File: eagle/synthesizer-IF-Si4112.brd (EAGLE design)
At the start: 34 x 31 mm, 39 parts, among them J1 142-0701-851, J3 142-0701-851, Q1 PMOS, U1 SI4112, X1 ECS-TXO-3225

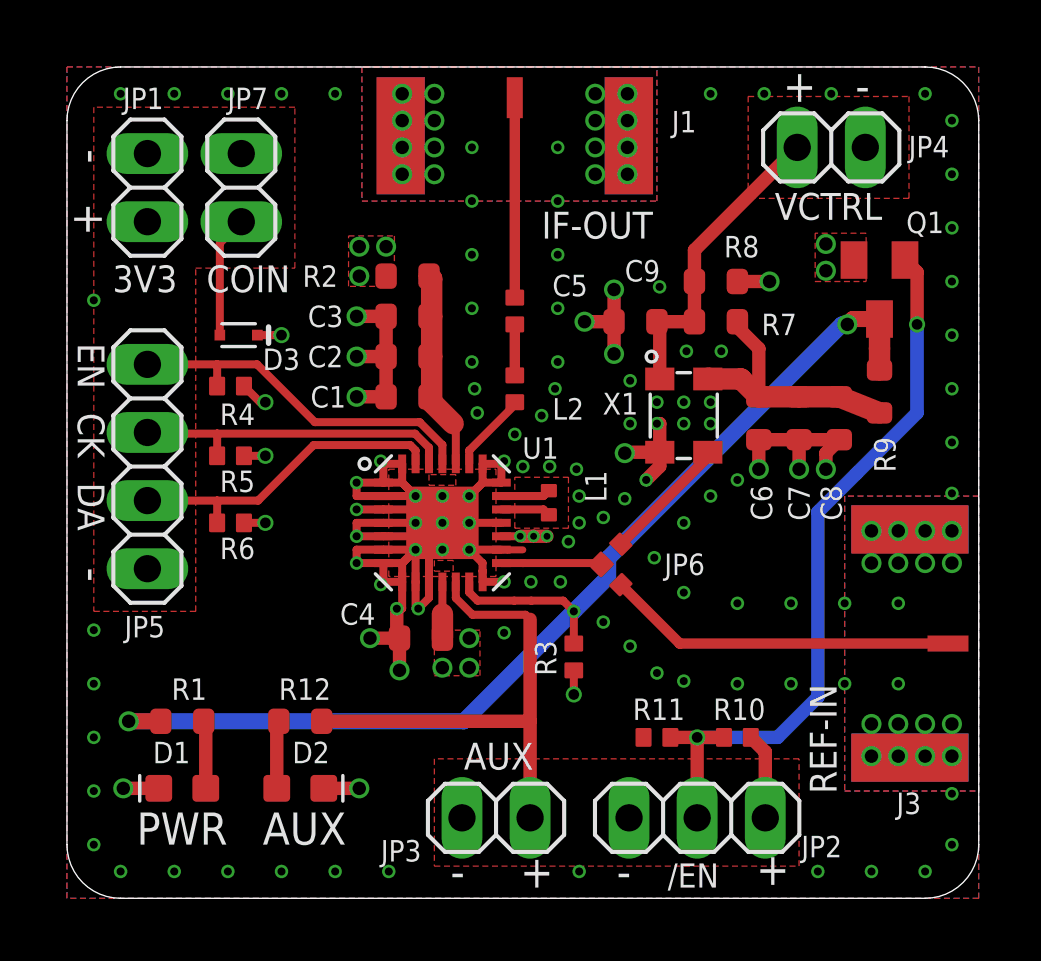
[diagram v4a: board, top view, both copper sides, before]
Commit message: Si4112 add 1u cap
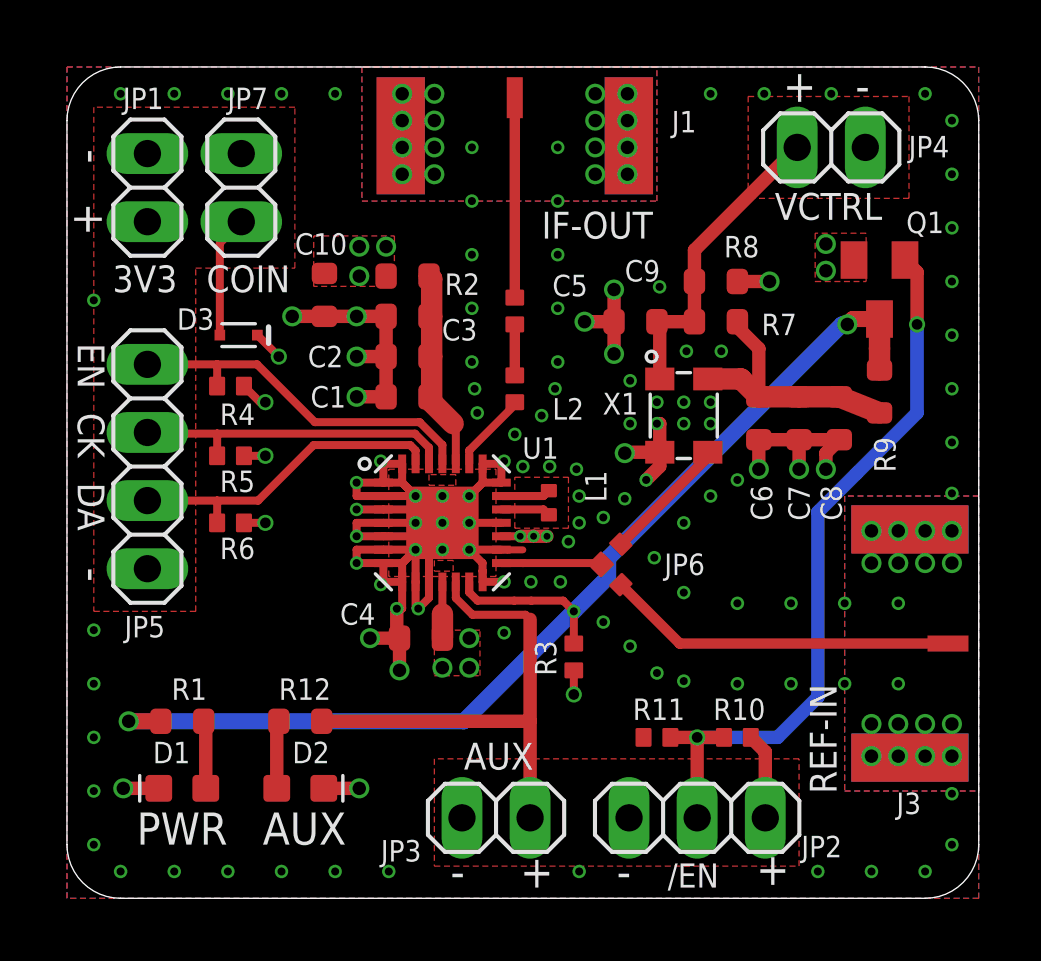
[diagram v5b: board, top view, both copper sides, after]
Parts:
- added C10: 1u, oresat-rcl:.0603-B-NOSILK
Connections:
- net +3V3: now also C10.1
- net GND: now also C10.2
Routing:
- net GND: track 69.2 -> 71.6 mm, vias 157 -> 158
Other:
- board text added: "IF Synthesizer Si4112 808 MHz L band LO PSAS / OreSat 2019-09-13 v1.0 E.M. - KJ7AOG"
- board text removed: "IF Synthesizer Si4112 808 MHz L band LO PSAS / OreSat 2019-09-11 v1.0 E.M. - KJ7AOG"
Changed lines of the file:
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@@
 808 MHz L band LO
 PSAS / OreSat
-2019-09-11  v1.0
+2019-09-13  v1.0
 E.M. - KJ7AOG</text>
-<text x="7.3" y="19.7" size="0.8" layer="21" font="vector" ratio="15">D3</text>
+<text x="4.1" y="21.2" size="0.8" layer="21" font="vector" ratio="15">D3</text>
 <text x="5.2" y="22.6" size="1" layer="21" font="vector" ratio="15">COIN</text>
 </plain>
@@
 </element>
 <element name="C3" library="oresat-rcl" package=".0603-B-NOSILK" value="NP" x="12.7" y="21.7" smashed="yes" rot="R180">
-<attribute name="NAME" x="10.3" y="22.1" size="0.8" layer="25" font="vector" ratio="15" rot="R180"/>
+<attribute name="NAME" x="15.3" y="21.6" size="0.8" layer="25" font="vector" ratio="15" rot="R180"/>
 <attribute name="NAME" x="12.7" y="21.7" size="0.3" layer="33" ratio="15" rot="R180" align="center"/>
 </element>
@@
 </element>
 <element name="R2" library="oresat-rcl" package=".0603-B-NOSILK" value="0" x="12.7" y="23.2" smashed="yes" rot="R180">
-<attribute name="NAME" x="10.1" y="23.6" size="0.8" layer="25" font="vector" ratio="15" rot="R180"/>
+<attribute name="NAME" x="15.4" y="23.3" size="0.8" layer="25" font="vector" ratio="15" rot="R180"/>
 <attribute name="NAME" x="12.7" y="23.2" size="0.3" layer="33" ratio="15" rot="R180" align="center"/>
 </element>
@@
 <attribute name="NAME" x="18.25" y="8.3" size="0.8" layer="25" font="vector" ratio="15" rot="R90"/>
 <attribute name="NAME" x="18.9" y="9" size="0.2" layer="33" ratio="15" rot="R90" align="center"/>
+</element>
+<element name="C10" library="oresat-rcl" package=".0603-B-NOSILK" value="1u" x="9.6" y="22.5" smashed="yes" rot="R270">
+<attribute name="NAME" x="8.5" y="24" size="0.8" layer="25" font="vector" ratio="15"/>
+<attribute name="NAME" x="9.6" y="22.5" size="0.3" layer="33" ratio="15" rot="R270" align="center"/>
 </element>
 </elements>
@@
 <via x="18.9" y="7.6" extent="1-16" drill="0.4"/>
 <wire x1="18.9" y1="8.5" x2="18.9" y2="7.6" width="0.3" layer="1"/>
+<contactref element="C10" pad="2"/>
+<wire x1="9.6" y1="21.7" x2="10.8" y2="21.7" width="0.5" layer="1"/>
+<via x="8.4" y="21.7" extent="1-16" drill="0.5"/>
+<wire x1="9.6" y1="21.7" x2="8.4" y2="21.7" width="0.5" layer="1"/>
 </signal>
 <signal name="/SEN">
@@
 <polygon width="0.3" layer="1" thermals="no">
 <vertex x="12.21" y="22.82"/>
-<vertex x="10.5" y="22.82"/>
-<vertex x="10.5" y="24.7"/>
+<vertex x="9.2" y="22.82"/>
+<vertex x="9.2" y="24.7"/>
 <vertex x="12.21" y="24.7"/>
 </polygon>
@@
 <wire x1="6.6" y1="19.1" x2="7.2" y2="18.5" width="0.3" layer="1"/>
 <wire x1="7.2" y1="18.5" x2="7.4" y2="18.5" width="0.3" layer="1"/>
-<via x="8" y="21" extent="1-16" drill="0.4"/>
-<wire x1="7.1" y1="21" x2="8" y2="21" width="0.3" layer="1"/>
+<via x="7.9" y="20.2" extent="1-16" drill="0.4"/>
+<wire x1="7.1" y1="21" x2="7.9" y2="20.2" width="0.3" layer="1"/>
+<contactref element="C10" pad="1"/>
 </signal>
 <signal name="VCTRL">
@@
 <wire x1="28.8" y1="18.7" x2="27.3" y2="18.7" width="0.8" layer="1"/>
 <wire x1="27.3" y1="18.7" x2="25.8" y2="18.7" width="0.8" layer="1"/>
-<wire x1="23.93" y1="19.4" x2="23.895" y2="19.365" width="0.8" layer="1"/>
 <wire x1="25.8" y1="20.5" x2="25" y2="21.3" width="0.5" layer="1"/>
 <wire x1="25" y1="21.5" x2="25" y2="21.3" width="0.5" layer="1"/>

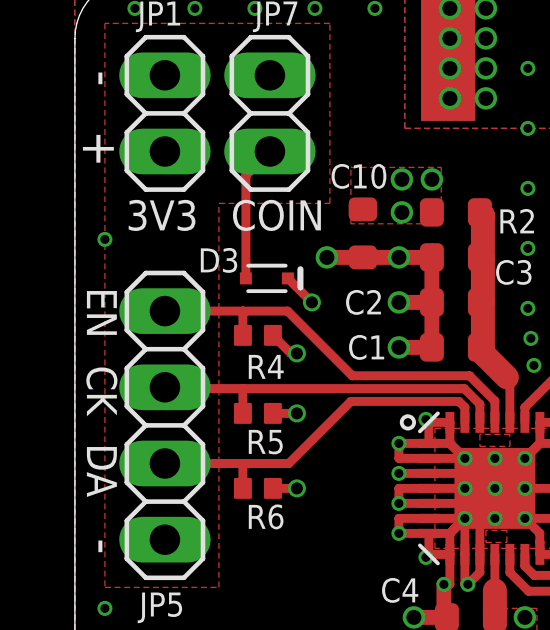
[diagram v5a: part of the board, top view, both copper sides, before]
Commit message: Synth LO Si4112, notes
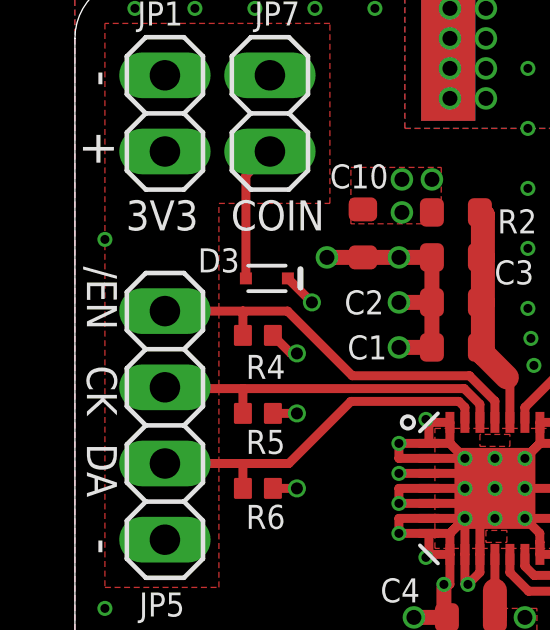
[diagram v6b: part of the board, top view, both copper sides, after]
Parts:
- R11: value NP -> 47k
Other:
- board text added: "IF Synthesizer Si4112 808 MHz L band LO PSAS / OreSat 2019-09-15 v1.0 E.M. - KJ7AOG"
- board text removed: "EN"
- board text removed: "IF Synthesizer Si4112 808 MHz L band LO PSAS / OreSat 2019-09-13 v1.0 E.M. - KJ7AOG"
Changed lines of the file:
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@@
 <text x="1.3" y="27.4" size="1.2" layer="21" font="vector" ratio="15" rot="R90">-</text>
 <text x="1.3" y="11.8" size="1.2" layer="21" font="vector" ratio="15" rot="R90">-</text>
-<text x="0.4" y="20.7" size="1" layer="21" font="vector" ratio="15" rot="SR270">EN</text>
+<text x="0.4" y="21.4" size="1" layer="21" font="vector" ratio="15" rot="SR270">/EN</text>
 <text x="0.4" y="18.1" size="1" layer="21" font="vector" ratio="15" rot="SR270">CK</text>
 <text x="0.4" y="15.5" size="1" layer="21" font="vector" ratio="15" rot="SR270">DA</text>
-<text x="28.8" y="11.8" size="1.7" layer="22" font="vector" ratio="15" rot="MR0">IF Synthesizer Si4112
+<text x="28.8" y="11.4" size="1.7" layer="22" font="vector" ratio="15" rot="MR0">IF Synthesizer Si4112
 808 MHz L band LO
 PSAS / OreSat
-2019-09-13  v1.0
+2019-09-15  v1.0
 E.M. - KJ7AOG</text>
 <text x="4.1" y="21.2" size="0.8" layer="21" font="vector" ratio="15">D3</text>
@@
 <attribute name="NAME" x="12.7" y="23.2" size="0.3" layer="33" ratio="15" rot="R180" align="center"/>
 </element>
-<element name="R11" library="oresat-rcl" package=".0402-B-NOSILK" value="NP" x="22" y="6" smashed="yes">
+<element name="R11" library="oresat-rcl" package=".0402-B-NOSILK" value="47k" x="22" y="6" smashed="yes">
 <attribute name="NAME" x="21.1" y="6.65" size="0.8" layer="25" font="vector" ratio="15"/>
 <attribute name="NAME" x="22" y="6" size="0.2" layer="33" ratio="15" align="center"/>

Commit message: Synth Si4112 change default shutdown
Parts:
- R10: value NP -> 47k
- R11: value 47k -> NP
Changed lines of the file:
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@@
 <drawing>
 <settings>
-<setting alwaysvectorfont="yes"/>
+<setting alwaysvectorfont="no"/>
 <setting verticaltext="up"/>
 </settings>
@@
 <attribute name="NAME" x="12.7" y="23.2" size="0.3" layer="33" ratio="15" rot="R180" align="center"/>
 </element>
-<element name="R11" library="oresat-rcl" package=".0402-B-NOSILK" value="47k" x="22" y="6" smashed="yes">
+<element name="R11" library="oresat-rcl" package=".0402-B-NOSILK" value="NP" x="22" y="6" smashed="yes">
 <attribute name="NAME" x="21.1" y="6.65" size="0.8" layer="25" font="vector" ratio="15"/>
 <attribute name="NAME" x="22" y="6" size="0.2" layer="33" ratio="15" align="center"/>
@@
 <attribute name="POPULARITY" value="8" x="30.3" y="22.7" size="1.778" layer="27" rot="R180" display="off"/>
 </element>
-<element name="R10" library="oresat-rcl" package=".0402-B-NOSILK" value="NP" x="25" y="6" smashed="yes">
+<element name="R10" library="oresat-rcl" package=".0402-B-NOSILK" value="47k" x="25" y="6" smashed="yes">
 <attribute name="NAME" x="24.1" y="6.65" size="0.8" layer="25" font="vector" ratio="15"/>
 <attribute name="NAME" x="25" y="6" size="0.2" layer="33" ratio="15" align="center"/>

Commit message: synth-si4112 update values
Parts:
- C6: value 1u -> NP
- C7: value NP -> 22n
- C8: value NP -> 1u
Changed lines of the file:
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@@
 <attribute name="NAME" x="16.7" y="21.9" size="0.2" layer="33" ratio="15" rot="R90" align="center"/>
 </element>
-<element name="C6" library="oresat-rcl" package=".0603-B-NOSILK" value="1u" x="25.8" y="17.9" smashed="yes" rot="R270">
+<element name="C6" library="oresat-rcl" package=".0603-B-NOSILK" value="NP" x="25.8" y="17.9" smashed="yes" rot="R270">
 <attribute name="NAME" x="25.5" y="15.4" size="0.8" layer="25" font="vector" ratio="15" rot="R270"/>
 <attribute name="NAME" x="25.8" y="17.9" size="0.3" layer="33" ratio="15" rot="R270" align="center"/>
 </element>
-<element name="C7" library="oresat-rcl" package=".0603-B-NOSILK" value="NP" x="27.3" y="17.9" smashed="yes" rot="R270">
+<element name="C7" library="oresat-rcl" package=".0603-B-NOSILK" value="22n" x="27.3" y="17.9" smashed="yes" rot="R270">
 <attribute name="NAME" x="26.9" y="15.4" size="0.8" layer="25" font="vector" ratio="15" rot="R270"/>
 <attribute name="NAME" x="27.3" y="17.9" size="0.3" layer="33" ratio="15" rot="R270" align="center"/>
 </element>
-<element name="C8" library="oresat-rcl" package=".0603-B-NOSILK" value="NP" x="28.8" y="17.9" smashed="yes" rot="R270">
+<element name="C8" library="oresat-rcl" package=".0603-B-NOSILK" value="1u" x="28.8" y="17.9" smashed="yes" rot="R270">
 <attribute name="NAME" x="28.1" y="15.4" size="0.8" layer="25" font="vector" ratio="15" rot="R270"/>
 <attribute name="NAME" x="28.8" y="17.9" size="0.3" layer="33" ratio="15" rot="R270" align="center"/>
